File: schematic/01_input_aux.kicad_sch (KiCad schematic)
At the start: 22 parts, among them J101 24.243.1 RED, J102 24.243.2 BLACK, U101 TPS259470LRPWR, U102 TPS54302DDCR

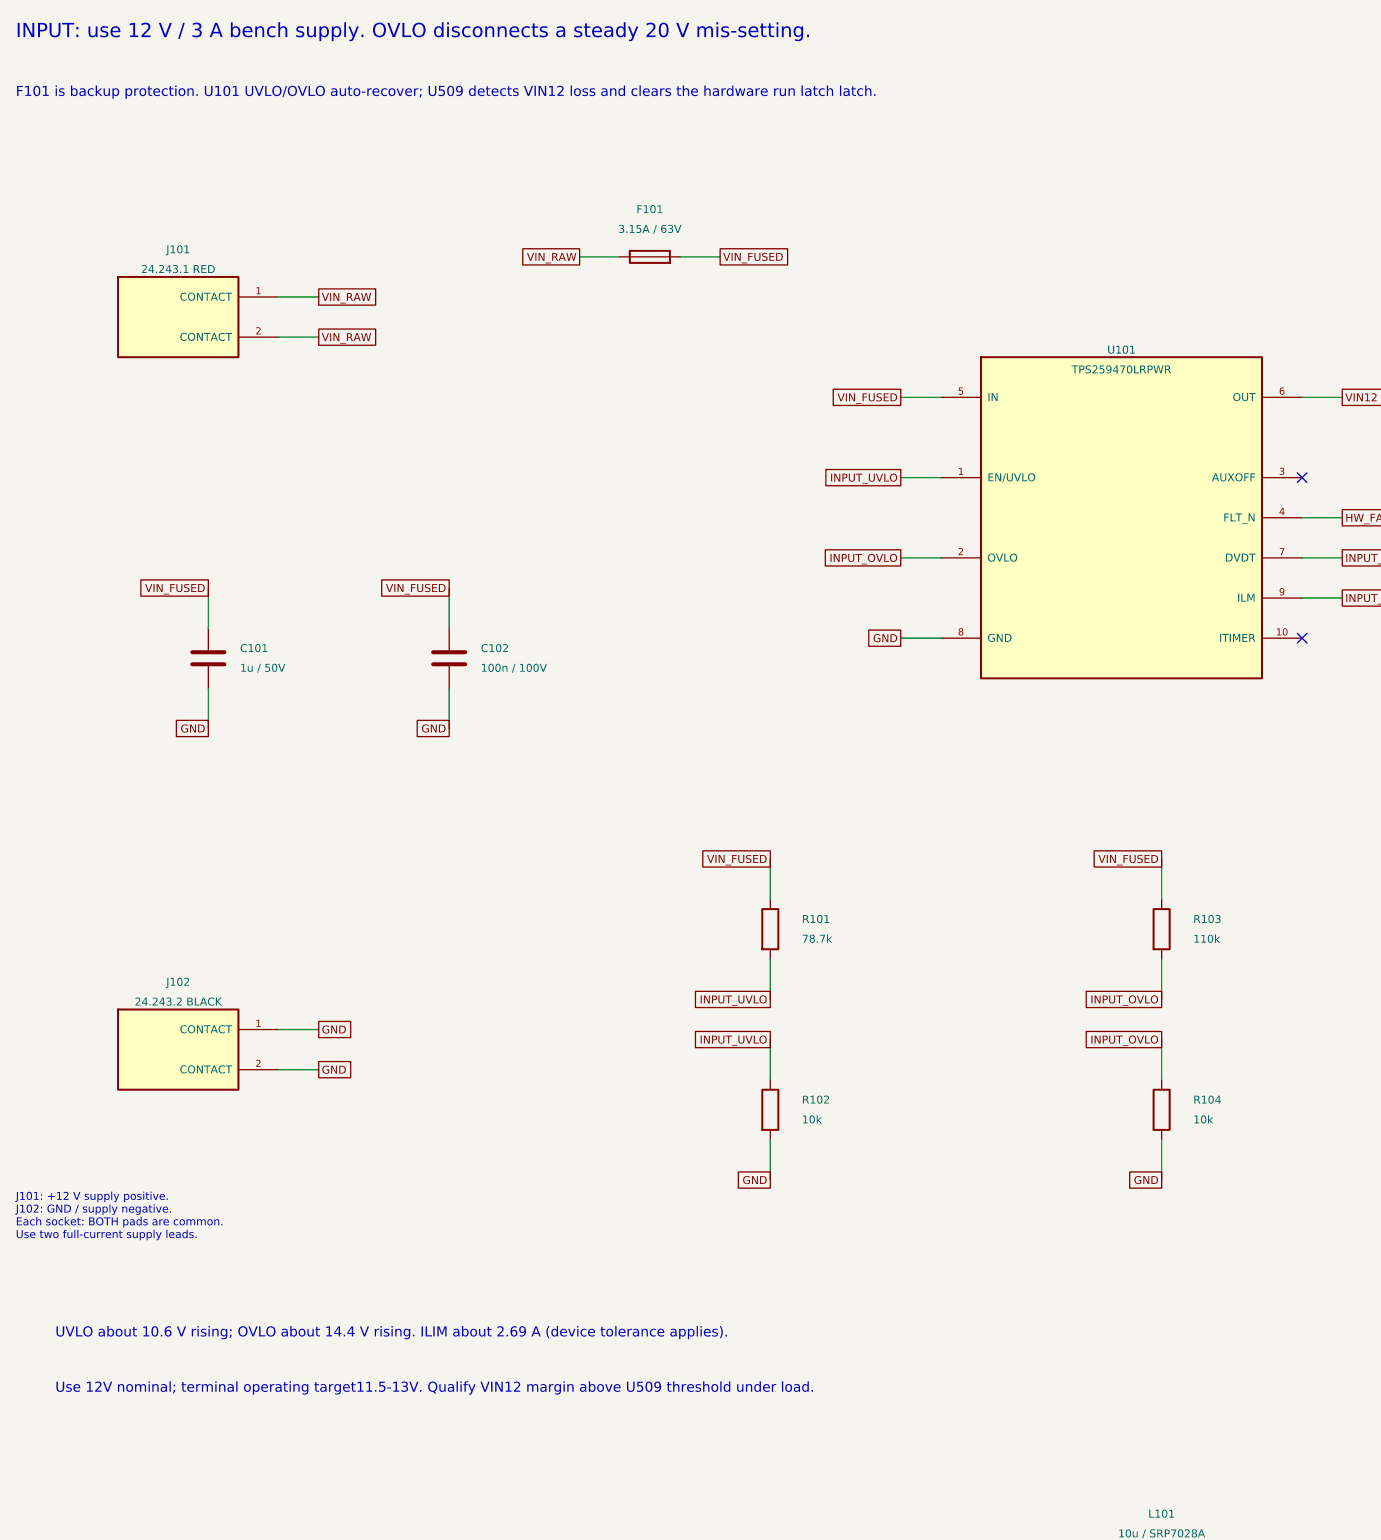
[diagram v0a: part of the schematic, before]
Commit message: Decouple DUT reset and input diagnostics from power interlocks
Use explicit manual, ZedBoard, and Pico reset requests. Route input-voltage validity to telemetry while retaining protective power interlocks. Synchronize requirements, schematic exports, BOM, and verification evidence.
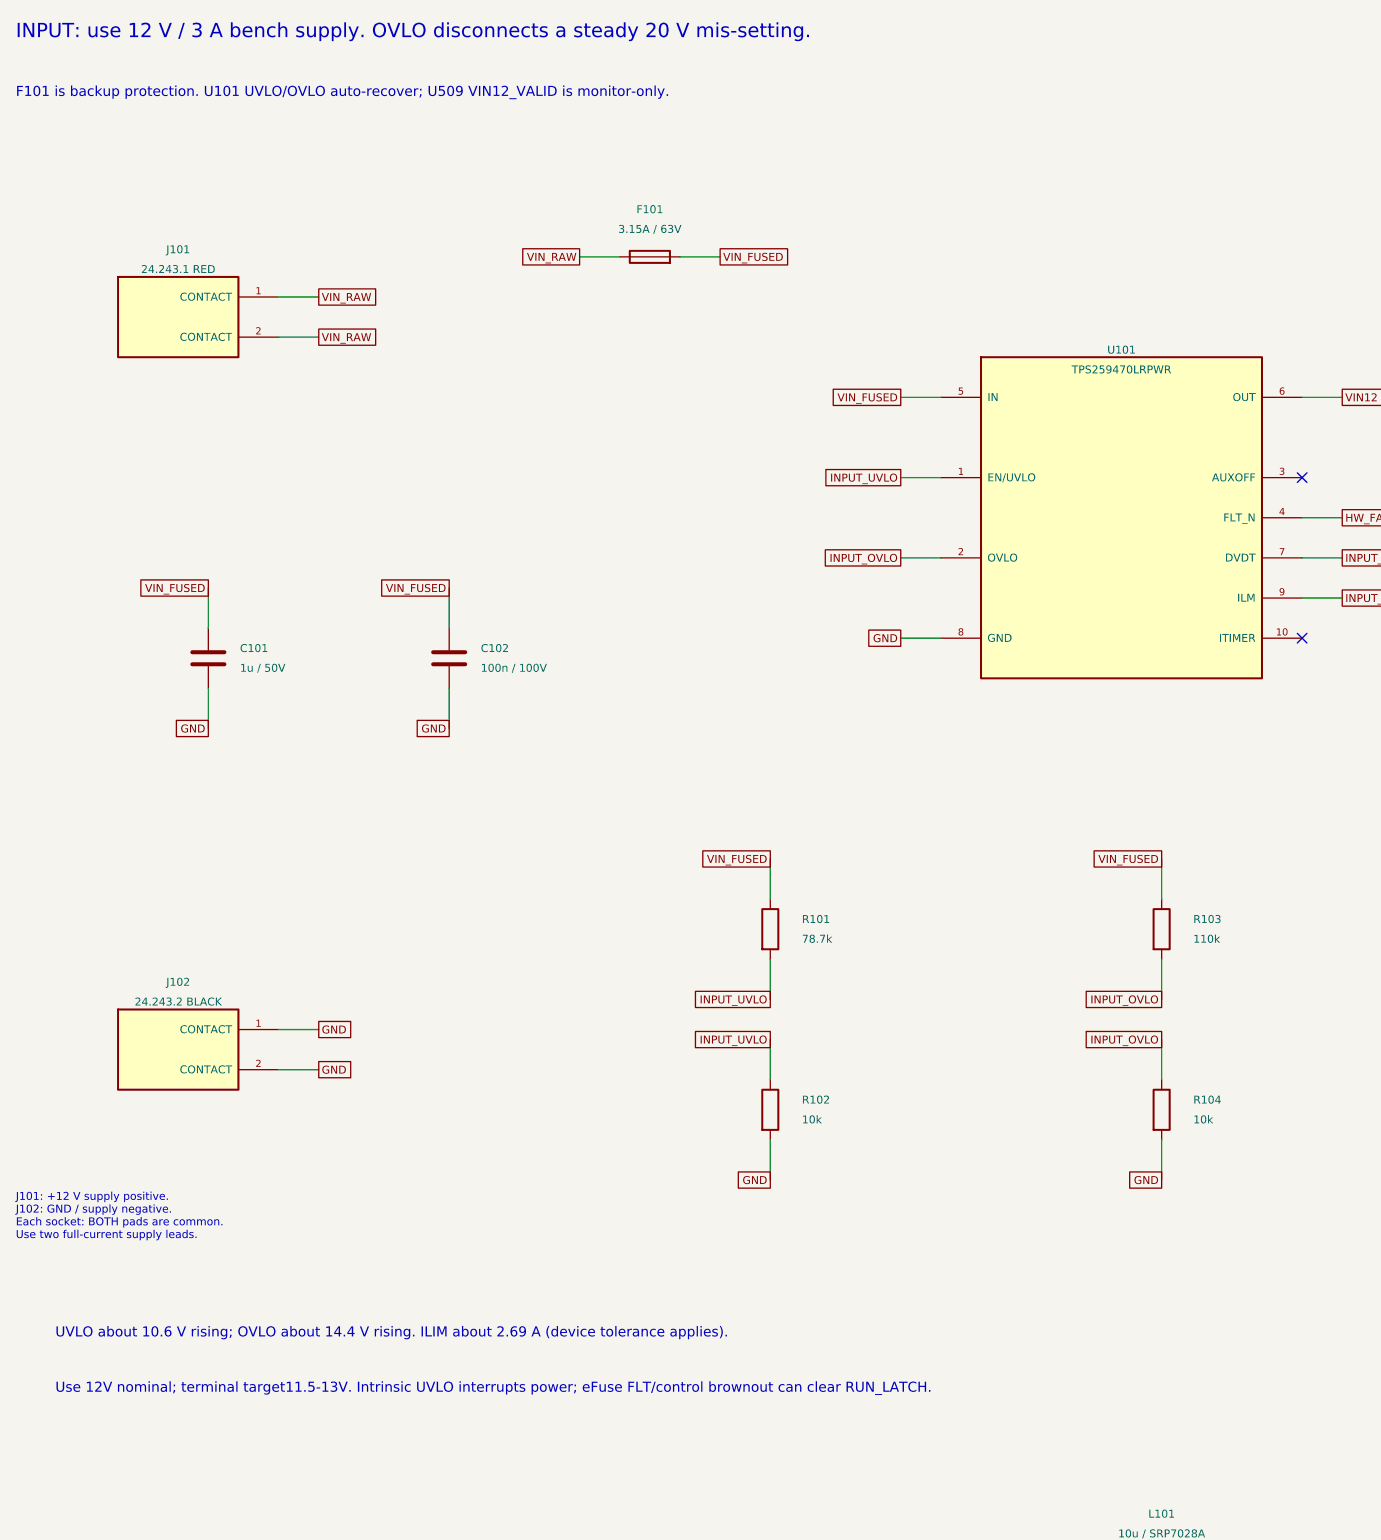
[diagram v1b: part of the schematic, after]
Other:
- note added: "F101 is backup protection. U101 UVLO/OVLO auto-recover; U509 VIN12_VALID is monitor-only."
- note added: "Use 12V nominal; terminal target11.5-13V. Intrinsic UVLO interrupts power; eFuse FLT/control brownout can clear RUN_LATCH."
- note removed: "F101 is backup protection. U101 UVLO/OVLO auto-recover; U509 detects VIN12 loss and clears the hardware run latch latch."
- note removed: "Use 12V nominal; terminal operating target11.5-13V. Qualify VIN12 margin above U509 threshold under load."
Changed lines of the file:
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@@
 (kicad_sch (version 20250114) (generator "eeschema") (generator_version "10.0")
  (paper "A3")
-        (title_block (title "01 | Protected input and auxiliary supply") (date "2026-09-19") (rev "V2")
+        (title_block (title "01 | Protected input and auxiliary supply") (date "2026-09-20") (rev "V2")
         (company "Sphinx | Programmable power test board")
         (comment 1 "Review package: PCB, PI, SI, thermal and ASIC limits require qualification")
@@
         (comment 3 "Author: Yuchen Mei"))
         (text "INPUT: use 12 V / 3 A bench supply. OVLO disconnects a steady 20 V mis-setting." (at 15 15 0) (effects (font (size 1.8 1.8)) (justify left top) ))
-(text "F101 is backup protection. U101 UVLO/OVLO auto-recover; U509 detects VIN12 loss and clears the hardware run latch latch." (at 15 23 0) (effects (font (size 1.27 1.27)) (justify left top) ))
+(text "F101 is backup protection. U101 UVLO/OVLO auto-recover; U509 VIN12_VALID is monitor-only." (at 15 23 0) (effects (font (size 1.27 1.27)) (justify left top) ))
 (symbol (lib_id "Sphinx_V2:Banana_4mm_TwoLegs") (at 35.56 52.07 0) (unit 1) (exclude_from_sim no) (in_bom yes) (on_board yes) (dnp no)
 (property "Reference" "J101" (at 35.56 43.53 0) (effects (font (size 1.0 1.0))  ))
@@
 (global_label "GND" (shape passive) (at 350.52 82.55 180) (effects (font (size 1.0 1.0)) (justify right) ) (property "Intersheetrefs" "${INTERSHEET_REFS}" (at 350.52 82.55 180) (effects (font (size 0.8 0.8))  (hide yes))))
 (text "UVLO about 10.6 V rising; OVLO about 14.4 V rising. ILIM about 2.69 A (device tolerance applies)." (at 20 180 0) (effects (font (size 1.27 1.27)) (justify left top) ))
-(text "Use 12V nominal; terminal operating target11.5-13V. Qualify VIN12 margin above U509 threshold under load." (at 20 187 0) (effects (font (size 1.27 1.27)) (justify left top) ))
+(text "Use 12V nominal; terminal target11.5-13V. Intrinsic UVLO interrupts power; eFuse FLT/control brownout can clear RUN_LATCH." (at 20 187 0) (effects (font (size 1.27 1.27)) (justify left top) ))
 (symbol (lib_id "Sphinx_V2:TPS54302") (at 90.17 228.6 0) (unit 1) (exclude_from_sim no) (in_bom yes) (on_board yes) (dnp no)
 (property "Reference" "U102" (at 90.17 212.44 0) (effects (font (size 1.0 1.0))  ))
